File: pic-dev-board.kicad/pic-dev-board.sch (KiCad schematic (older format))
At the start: 44 parts, among them J1 Conn_01x03_Male, J13 Conn_01x06_Male, J15 Barrel_Jack_Switch, J16 RUN/~PGM, J17 I2C, J18 GP1(RA1)/RB6, J19 GP2(RA2)/RB4, J2 Conn_01x03_Male, J20 Conn_01x06_Male, J3 Conn_01x03_Male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

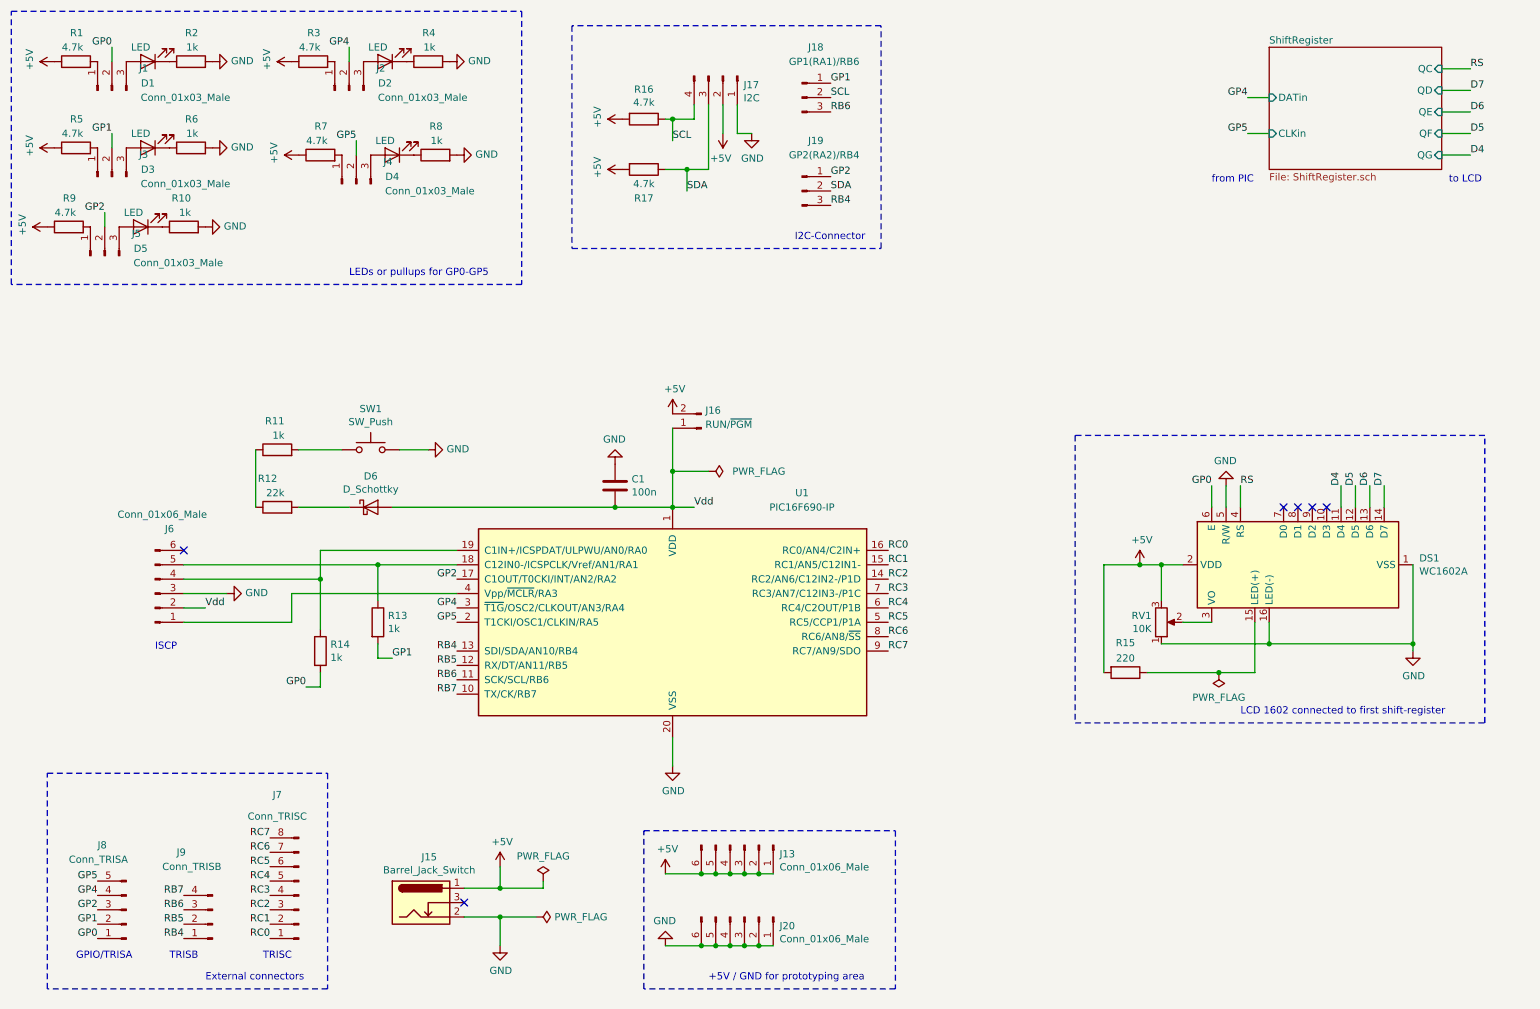
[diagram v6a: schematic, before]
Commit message: added labels, algined parts
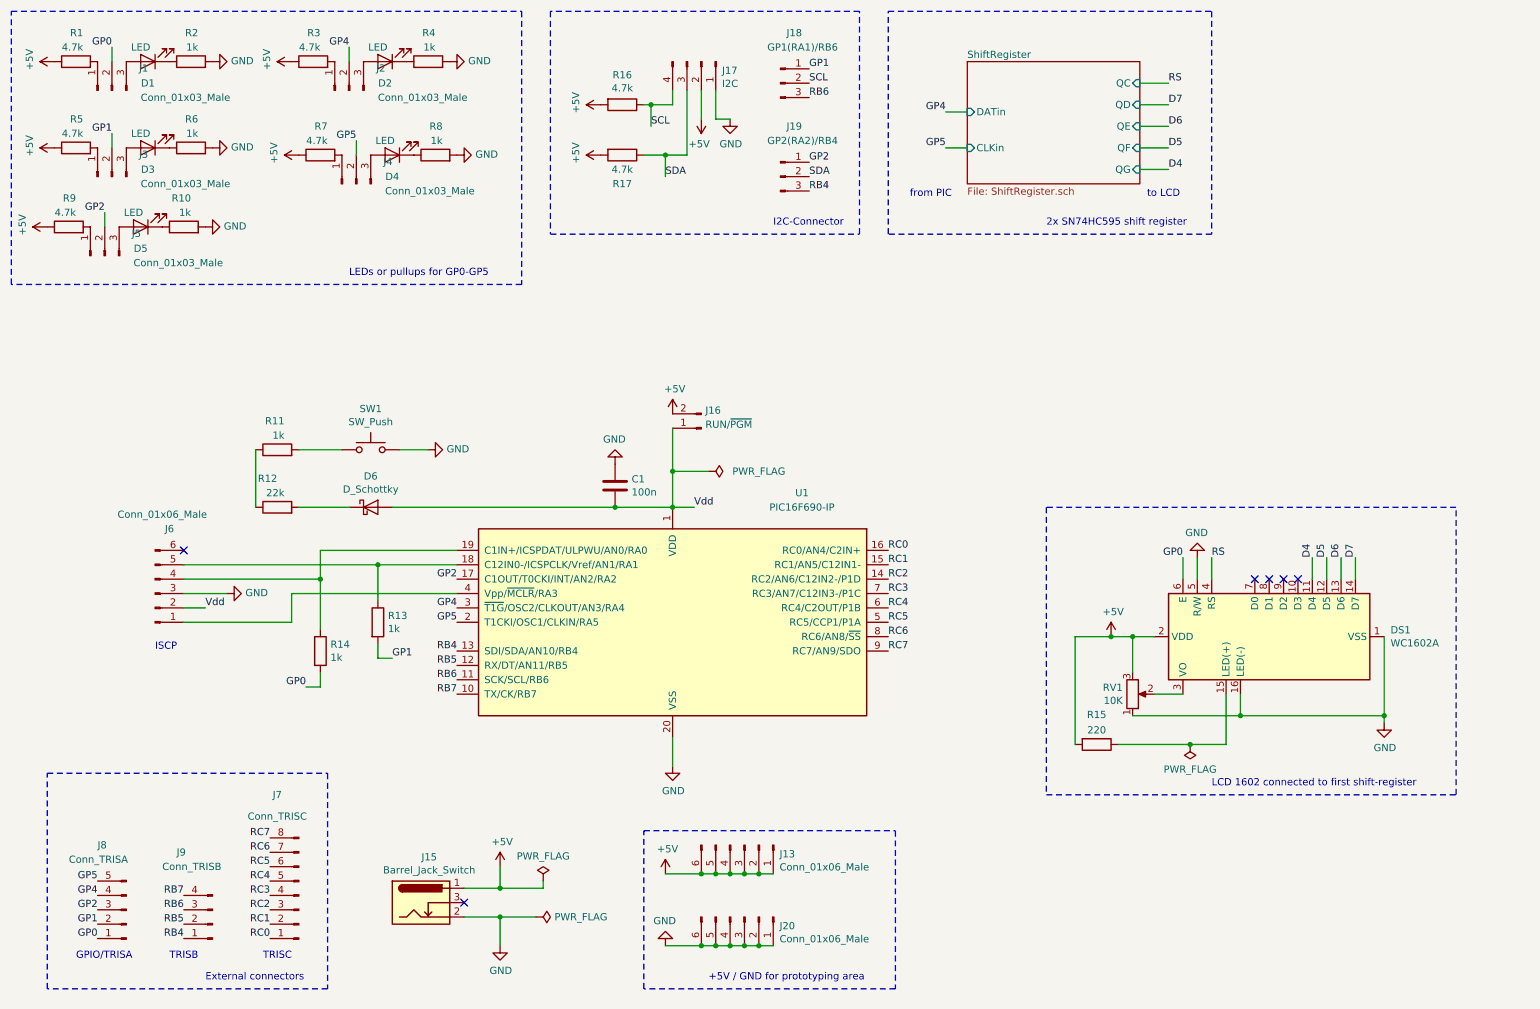
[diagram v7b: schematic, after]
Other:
- note added: "2x SN74HC595 shift register"
- moved on the sheet: DS1, J17, J18, J19, R15, R16, R17, RV1

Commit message: added footprints
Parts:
- D1, D2, D3, D4, D5: footprint LED_THT:LED_D3.0mm -> user:LED_1206_3216_Pad1.7x1.75mm_BB
- J1, J18, J19, J2, J3, J4, J5: footprint (none) -> Connector_PinHeader_2.54mm:PinHeader_1x03_P2.54mm_Vertical
- J13, J20: footprint (none) -> Connector_PinHeader_2.54mm:PinHeader_1x06_P2.54mm_Vertical
- J15: footprint (none) -> Connector_BarrelJack:BarrelJack_CUI_PJ-063AH_Horizontal
- J16: footprint (none) -> Connector_PinHeader_2.54mm:PinHeader_1x02_P2.54mm_Vertical
- J17, J9: footprint (none) -> Connector_PinHeader_2.54mm:PinHeader_1x04_P2.54mm_Vertical
- J7: footprint (none) -> Connector_PinHeader_2.54mm:PinHeader_1x08_P2.54mm_Vertical
- R1, R10, R11, R12, R13, R14, R2, R3, R4, R5, R6, R7, R8, R9: footprint Resistor_THT:R_Axial_DIN0207_L6.3mm_D2.5mm_P10.16mm_Horizontal -> user:R_1206_3216_Pad1.7x1.75mm_BB
- R15, R16, R17: footprint (none) -> user:R_1206_3216_Pad1.7x1.75mm_BB
- RV1: footprint (none) -> Potentiometer_THT:Potentiometer_Vishay_T73XW_Horizontal
- U1: footprint (none) -> Package_DIP:DIP-20_W7.62mm_Socket
